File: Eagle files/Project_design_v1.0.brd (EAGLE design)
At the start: 100 x 80 mm, 4 parts

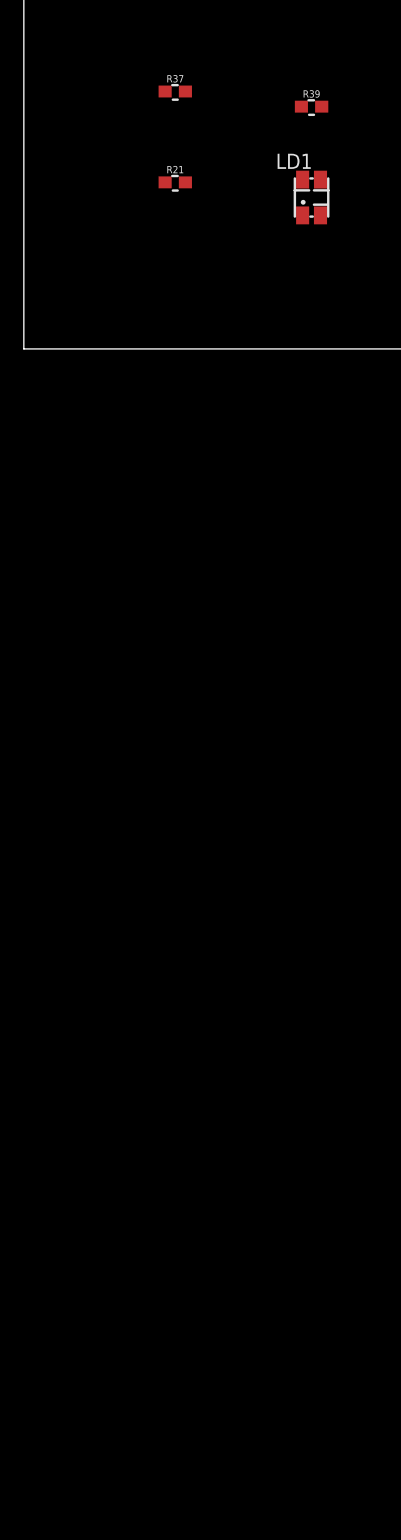
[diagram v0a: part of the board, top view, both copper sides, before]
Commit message: schematic des temperature, soil moisture, led, brightness sensor
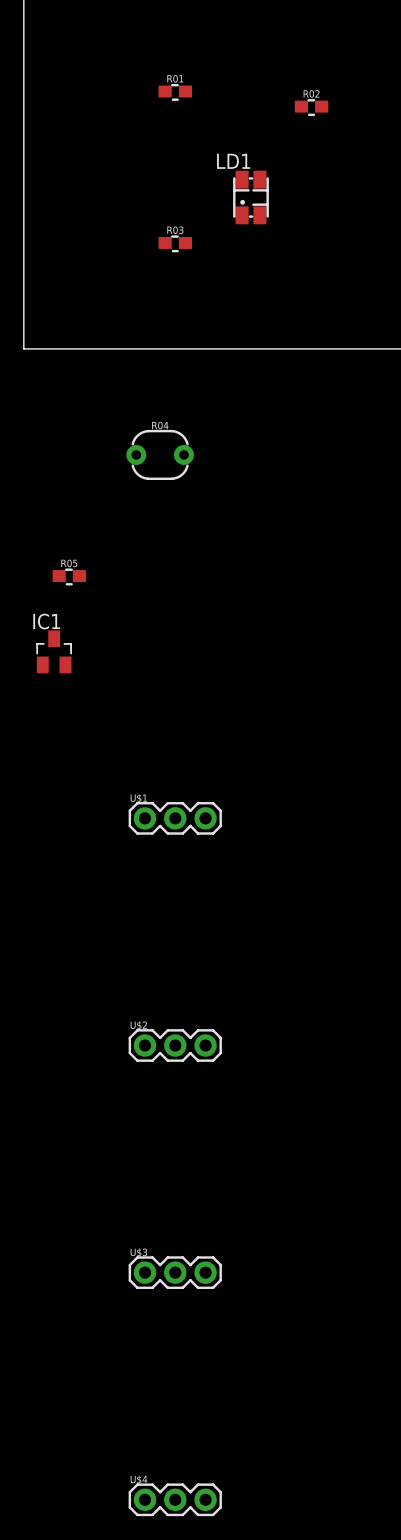
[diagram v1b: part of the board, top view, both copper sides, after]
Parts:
- removed R21: OR, custom_part:0603
- added IC1: LM50, linear:SOT23
- added R03: 2K, custom_part:0603
- added R04: PHOTOCELLPTH, SparkFun-Sensors:PHOTOCELL
- added R05: 10K, custom_part:0603
- added U$1, U$2, U$3, U$4: SOIL_MOISTURE, potentiometer:SOIL_MOISTURE
- R01: value 100R -> 3K
- R02: value 100R -> 2K
- moved LD1 5.08 mm to (19.1, 12.7)
- renumbered R37 to R01, R39 to R02
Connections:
- removed net MUX_DIS: R21.2
- new net GND: R05.1
- new net MOISTURE1: U$1.3
- new net MOISTURE2: U$2.3
- new net MOISTURE3: U$3.3
- new net MOISTURE4: U$4.3
- new net N$1: LD1.2, R03.1
- new net N$2: U$1.2
- new net N$3: U$2.2
- new net N$4: IC1.3
- new net N$5: U$3.2
- new net N$6: U$4.2
- new net PHOTOCELL_READ: R04.1, R05.2
- new net TEMP_READ: IC1.2
- net 3.3V: now also IC1.1, R04.2, U$1.1, U$2.1, U$3.1, U$4.1
- net LED_B: now also R03.2; no longer LD1.2
- net LED_R: no longer R21.1
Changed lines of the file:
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@@
 </autorouter>
 <elements>
-<element name="LD1" library="Semicond" package="PLCC-4" value="ASMB-MTB0-0A3A2PLCC-4" x="24.13" y="12.7">
-<attribute name="CODE" value="2401105" x="24.13" y="12.7" size="1.778" layer="27" display="off"/>
-<attribute name="DISTRIBUTOR" value="Farnell" x="24.13" y="12.7" size="1.778" layer="27" display="off"/>
-<attribute name="LINK" value="http://ch.farnell.com/fr-CH/broadcom-limited/asmb-mtb0-0a3a2/led-rgb-plcc4-surface-noire/dp/2401105" x="24.13" y="12.7" size="1.778" layer="27" display="off"/>
-<attribute name="PARTNO" value="ASMB-MTB0-0A3A2" x="24.13" y="12.7" size="1.778" layer="27" display="off"/>
-<attribute name="REFERENCE" value="ASMB-MTB0-0A3A2" x="24.13" y="12.7" size="1.778" layer="27" display="off"/>
-<attribute name="UNIT_PRICE" value="0.332" x="24.13" y="12.7" size="1.778" layer="27" display="off"/>
+<element name="LD1" library="Semicond" package="PLCC-4" value="ASMB-MTB0-0A3A2PLCC-4" x="19.05" y="12.7">
+<attribute name="CODE" value="2401105" x="19.05" y="12.7" size="1.778" layer="27" display="off"/>
+<attribute name="DISTRIBUTOR" value="Farnell" x="19.05" y="12.7" size="1.778" layer="27" display="off"/>
+<attribute name="LINK" value="http://ch.farnell.com/fr-CH/broadcom-limited/asmb-mtb0-0a3a2/led-rgb-plcc4-surface-noire/dp/2401105" x="19.05" y="12.7" size="1.778" layer="27" display="off"/>
+<attribute name="PARTNO" value="ASMB-MTB0-0A3A2" x="19.05" y="12.7" size="1.778" layer="27" display="off"/>
+<attribute name="REFERENCE" value="ASMB-MTB0-0A3A2" x="19.05" y="12.7" size="1.778" layer="27" display="off"/>
+<attribute name="UNIT_PRICE" value="0.332" x="19.05" y="12.7" size="1.778" layer="27" display="off"/>
 </element>
-<element name="R21" library="custom_part" package="0603" value="OR" x="12.7" y="13.97">
-<attribute name="PARTNO" value="ERJ-PA3F1002V" x="12.7" y="13.97" size="1.778" layer="27" display="off"/>
-</element>
-<element name="R37" library="custom_part" package="0603" value="100R" x="12.7" y="21.59">
+<element name="R01" library="custom_part" package="0603" value="3K" x="12.7" y="21.59">
 <attribute name="PARTNO" value="ERJ-PA3F1002V" x="12.7" y="21.59" size="1.778" layer="27" display="off"/>
 </element>
-<element name="R39" library="custom_part" package="0603" value="100R" x="24.13" y="20.32">
+<element name="R02" library="custom_part" package="0603" value="2K" x="24.13" y="20.32">
 <attribute name="PARTNO" value="ERJ-PA3F1002V" x="24.13" y="20.32" size="1.778" layer="27" display="off"/>
 </element>
+<element name="R03" library="custom_part" package="0603" value="2K" x="12.7" y="8.89">
+<attribute name="PARTNO" value="ERJ-PA3F1002V" x="12.7" y="8.89" size="1.778" layer="27" display="off"/>
+</element>
+<element name="R04" library="SparkFun-Sensors" library_urn="urn:adsk.eagle:library:534" package="PHOTOCELL" package3d_urn="urn:adsk.eagle:package:39940/1" value="PHOTOCELLPTH" x="11.43" y="-8.89">
+<attribute name="PROD_ID" value="COMP-09129" x="11.43" y="-8.89" size="1.778" layer="27" display="off"/>
+<attribute name="SF_ID" value="SEN-09088" x="11.43" y="-8.89" size="1.778" layer="27" display="off"/>
+</element>
+<element name="R05" library="custom_part" package="0603" value="10K" x="3.81" y="-19.05">
+<attribute name="PARTNO" value="ERJ-PA3F1002V" x="3.81" y="-19.05" size="1.778" layer="27" display="off"/>
+</element>
+<element name="IC1" library="linear" library_urn="urn:adsk.eagle:library:262" package="SOT23" package3d_urn="urn:adsk.eagle:package:16489/2" value="LM50" x="2.54" y="-25.4"/>
+<element name="U$1" library="potentiometer" package="SOIL_MOISTURE" value="SOIL_MOISTURE" x="12.7" y="-39.37"/>
+<element name="U$2" library="potentiometer" package="SOIL_MOISTURE" value="SOIL_MOISTURE" x="12.7" y="-58.42"/>
+<element name="U$3" library="potentiometer" package="SOIL_MOISTURE" value="SOIL_MOISTURE" x="12.7" y="-77.47"/>
+<element name="U$4" library="potentiometer" package="SOIL_MOISTURE" value="SOIL_MOISTURE" x="12.7" y="-96.52"/>
 </elements>
 <signals>
 <signal name="3.3V">
 <contactref element="LD1" pad="1"/>
-</signal>
-<signal name="MUX_DIS">
-<contactref element="R21" pad="2"/>
+<contactref element="R04" pad="2"/>
+<contactref element="IC1" pad="1"/>
+<contactref element="U$1" pad="1"/>
+<contactref element="U$2" pad="1"/>
+<contactref element="U$3" pad="1"/>
+<contactref element="U$4" pad="1"/>
+<wire x1="10.16" y1="-77.47" x2="10.16" y2="-96.52" width="0" layer="19" extent="1-1"/>
+<wire x1="10.16" y1="-58.42" x2="10.16" y2="-77.47" width="0" layer="19" extent="1-1"/>
+<wire x1="10.16" y1="-39.37" x2="10.16" y2="-58.42" width="0" layer="19" extent="1-1"/>
+<wire x1="1.59" y1="-26.5" x2="10.16" y2="-39.37" width="0" layer="19" extent="1-1"/>
+<wire x1="13.43" y1="-8.89" x2="1.59" y2="-26.5" width="0" layer="19" extent="1-1"/>
+<wire x1="18.3" y1="11.2" x2="13.43" y2="-8.89" width="0" layer="19" extent="1-1"/>
 </signal>
 <signal name="N$34">
 <contactref element="LD1" pad="3"/>
-<contactref element="R37" pad="1"/>
-<wire x1="11.85" y1="21.59" x2="24.88" y2="14.2" width="0" layer="19" extent="1-1"/>
+<contactref element="R01" pad="1"/>
+<wire x1="11.85" y1="21.59" x2="19.8" y2="14.2" width="0" layer="19" extent="1-1"/>
 </signal>
 <signal name="N$35">
 <contactref element="LD1" pad="4"/>
-<contactref element="R39" pad="1"/>
-<wire x1="23.28" y1="20.32" x2="24.88" y2="11.2" width="0" layer="19" extent="1-1"/>
+<contactref element="R02" pad="1"/>
+<wire x1="23.28" y1="20.32" x2="19.8" y2="11.2" width="0" layer="19" extent="1-1"/>
+</signal>
+<signal name="LED_G">
+<contactref element="R01" pad="2"/>
+</signal>
+<signal name="LED_R">
+<contactref element="R02" pad="2"/>
+</signal>
+<signal name="N$1">
+<contactref element="LD1" pad="2"/>
+<contactref element="R03" pad="1"/>
+<wire x1="11.85" y1="8.89" x2="18.3" y2="14.2" width="0" layer="19" extent="1-1"/>
 </signal>
 <signal name="LED_B">
-<contactref element="LD1" pad="2"/>
+<contactref element="R03" pad="2"/>
 </signal>
-<signal name="LED_G">
-<contactref element="R37" pad="2"/>
+<signal name="PHOTOCELL_READ">
+<contactref element="R05" pad="2"/>
+<contactref element="R04" pad="1"/>
+<wire x1="9.43" y1="-8.89" x2="4.66" y2="-19.05" width="0" layer="19" extent="1-1"/>
 </signal>
-<signal name="LED_R">
-<contactref element="R39" pad="2"/>
-<contactref element="R21" pad="1"/>
-<wire x1="11.85" y1="13.97" x2="24.98" y2="20.32" width="0" layer="19" extent="1-1"/>
+<signal name="GND">
+<contactref element="R05" pad="1"/>
+</signal>
+<signal name="TEMP_READ">
+<contactref element="IC1" pad="2"/>
+</signal>
+<signal name="N$4">
+<contactref element="IC1" pad="3"/>
+</signal>
+<signal name="N$2">
+<contactref element="U$1" pad="2"/>
+</signal>
+<signal name="MOISTURE1">
+<contactref element="U$1" pad="3"/>
+</signal>
+<signal name="N$3">
+<contactref element="U$2" pad="2"/>
+</signal>
+<signal name="N$5">
+<contactref element="U$3" pad="2"/>
+</signal>
+<signal name="N$6">
+<contactref element="U$4" pad="2"/>
+</signal>
+<signal name="MOISTURE3">
+<contactref element="U$3" pad="3"/>
+</signal>
+<signal name="MOISTURE4">
+<contactref element="U$4" pad="3"/>
+</signal>
+<signal name="MOISTURE2">
+<contactref element="U$2" pad="3"/>
 </signal>
 </signals>
 </board>
 </drawing>
+<compatibility>
+<note version="8.2" severity="warning">
+Since Version 8.2, EAGLE supports online libraries. The ids
+of those online libraries will not be understood (or retained)
+with this version.
+</note>
+<note version="8.3" severity="warning">
+Since Version 8.3, EAGLE supports URNs for individual library
+assets (packages, symbols, and devices). The URNs of those assets
+will not be understood (or retained) with this version.
+</note>
+<note version="8.3" severity="warning">
+Since Version 8.3, EAGLE supports the association of 3D packages
+with devices in libraries, schematics, and board files. Those 3D
+packages will not be understood (or retained) with this version.
+</note>
+</compatibility>
 </eagle>

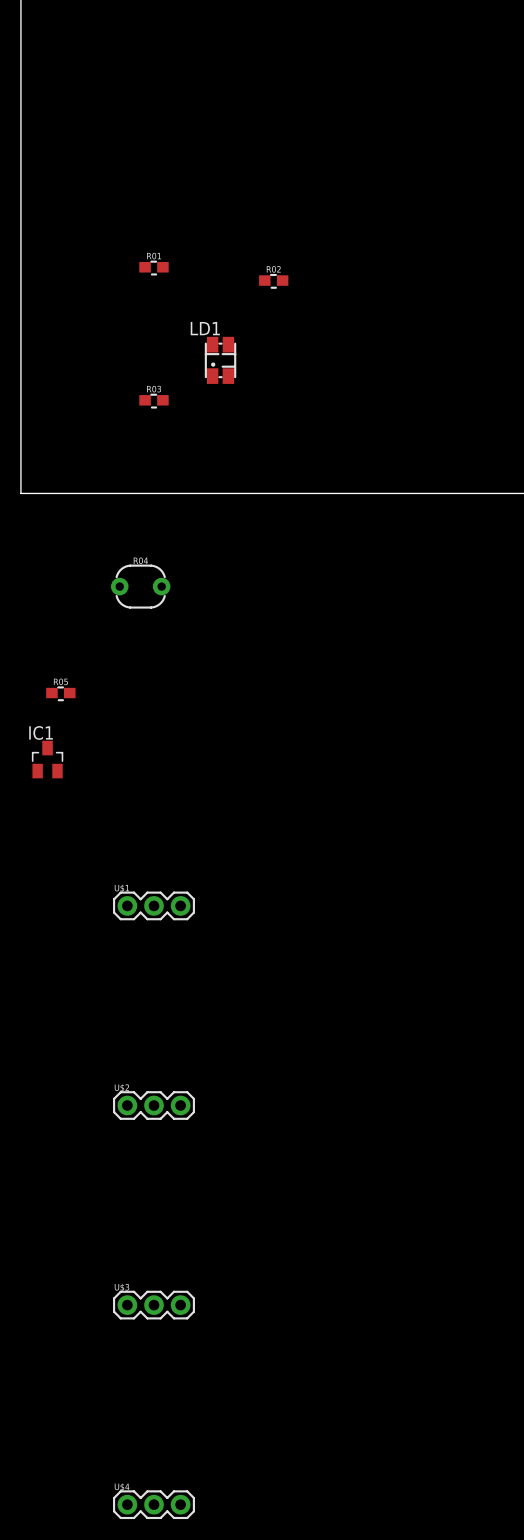
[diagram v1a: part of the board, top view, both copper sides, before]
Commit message: temperature sensor schmetatic & packages edited
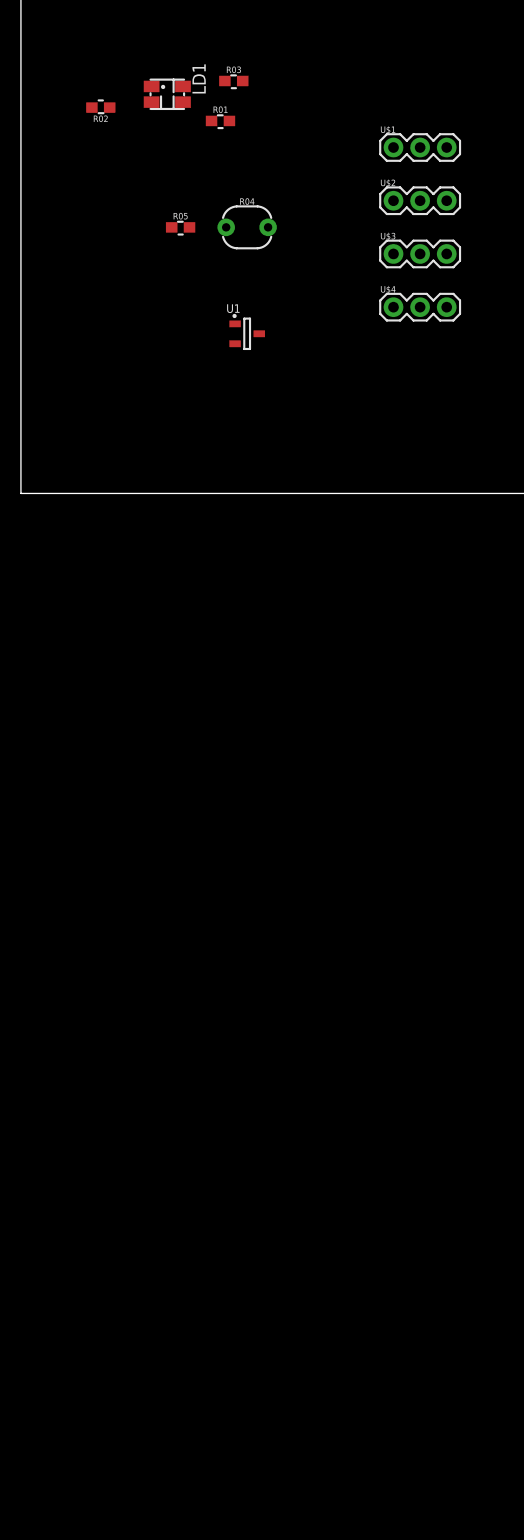
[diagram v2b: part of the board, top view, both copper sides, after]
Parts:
- removed IC1: LM50, linear:SOT23
- added U1: MCP9700T-E/TT, MCP9700T-E_TT:SOT95P237X112-3N
- moved U$4 117.1 mm to (38.1, 17.8)
- moved U$3 103.5 mm to (38.1, 22.9)
- moved U$2 90.0 mm to (38.1, 27.9)
- moved U$1 76.7 mm to (38.1, 33.0)
- moved R05 45.9 mm to (15.2, 25.4)
- moved R04 35.8 mm to (21.6, 25.4)
- moved R03 31.4 mm to (20.3, 39.4)
- moved LD1 25.9 mm to (14.0, 38.1), turned to 270 degrees
- moved R02 23.3 mm to (7.62, 36.8), turned to 180 degrees
- moved R01 15.3 mm to (19.1, 35.6)
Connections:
- removed net N$2: U$1.2
- removed net N$3: U$2.2
- removed net N$4: IC1.3
- removed net N$5: U$3.2
- removed net N$6: U$4.2
- net 3.3V: now also U1.1; no longer IC1.1
- net GND: now also U$1.2, U$2.2, U$3.2, U$4.2, U1.3
- net TEMP_READ: now also U1.2; no longer IC1.2

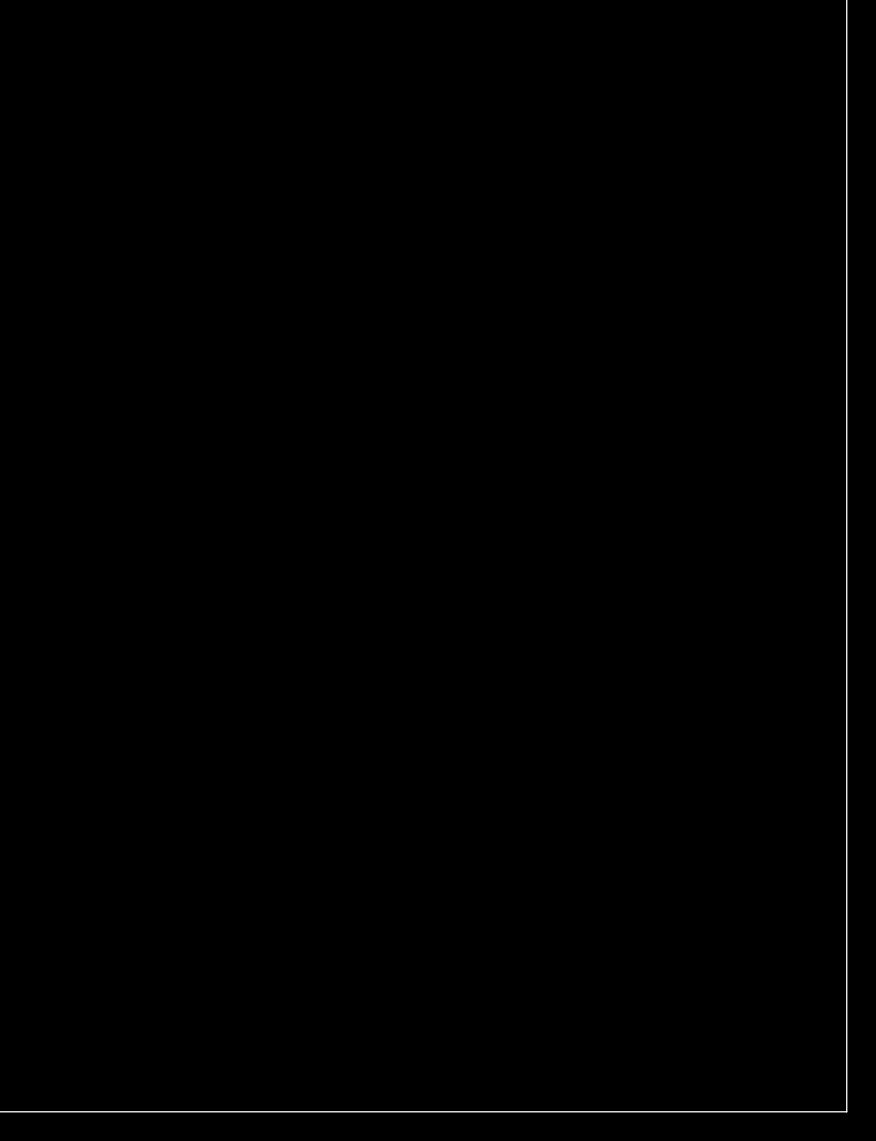
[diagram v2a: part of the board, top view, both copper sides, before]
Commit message: MCU, charging IC & power supply implemented on the eagle schematics
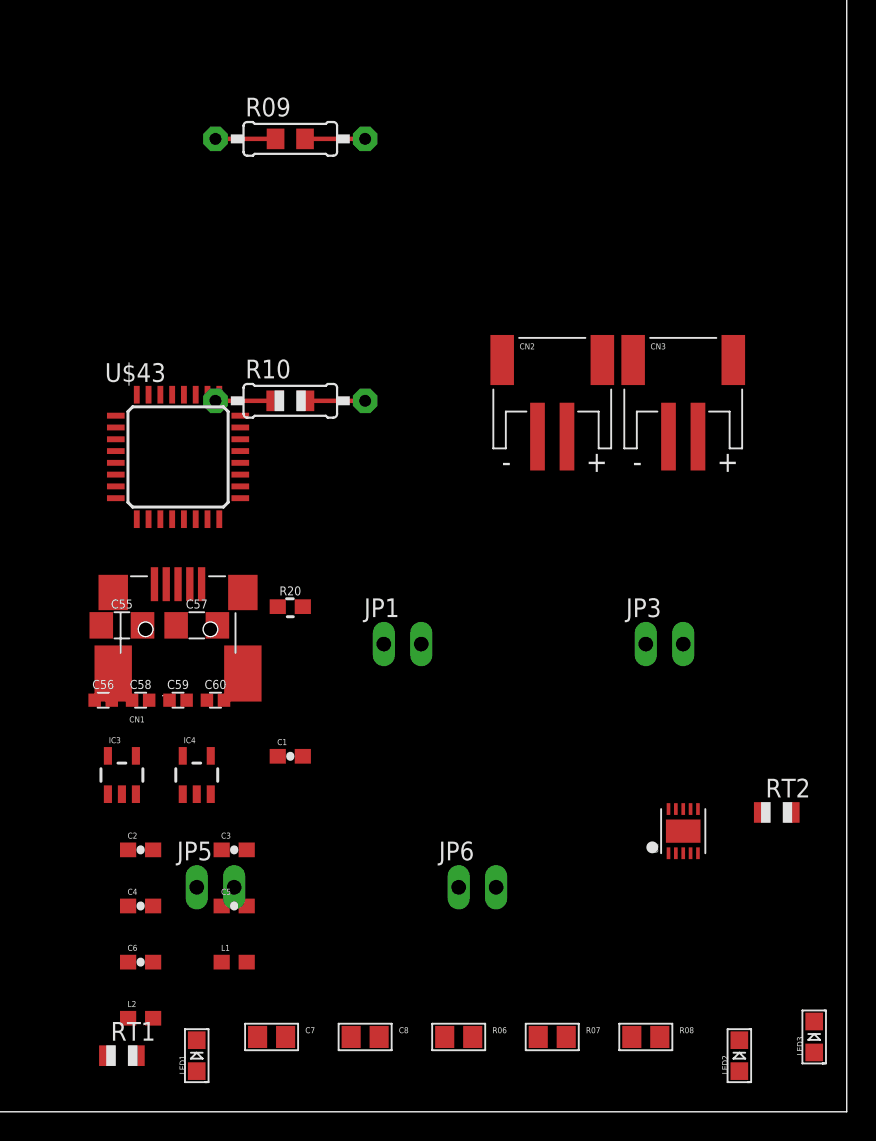
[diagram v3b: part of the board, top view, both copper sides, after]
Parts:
- added C1, C4: 2.2uF, SparkFun-Passives:0603-CAP
- added C2, C3, C5, C6: 10uF, SparkFun-Passives:0603-CAP
- added C55, C57: 10uF, custom_part:1206
- added C56, C58, C59, C60: 100n, custom_part:0402
- added C7, C8: 10uF, microbuilder:0805
- added CN1: USB, microbuilder:USB-MINIB_LARGER
- added CN2: BATT_IN_JST, microbuilder:JSTPH2
- added CN3: LOAD_JST, microbuilder:JSTPH2
- added IC3: TPS73250DBVT, TPS32xx:SOT23-5
- added IC4: TPS73233DBVT, TPS32xx:SOT23-5
- added JP1: PWR_IN_0.1, microbuilder:1X02_OVAL
- added JP3: LOAD_0.1, microbuilder:1X02_OVAL
- added JP5: BATT_IN_0.1, microbuilder:1X02_OVAL
- added JP6: STAT, microbuilder:1X02_OVAL
- added L1, L2: 3.3 uH, SparkFun-Passives:0603
- added LED1: STAT1-ORANGE, microbuilder:CHIPLED_0805
- added LED2: STAT2-GREEN, microbuilder:CHIPLED_0805
- added LED3: Power-RED, microbuilder:CHIPLED_0805
- added R06, R07, R08: 150, microbuilder:0805
- added R09: PROG, microbuilder:0805-THM
- added R10: 10K/THERM, adafruit:0805-THM
- added R20: 10K, custom_part:0603
- added RT1: 1K, adafruit:R0805
- added RT2: 150K, adafruit:R0805
- added U$43: STM32F042K6T6, stm32-microcontrollers:LQFP32-7X7
- added U2: MCP73833T-AMI/MF, microbuilder:DFN10_3X3MM
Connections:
- new net 5.0V: C7.1, CN1.VBUS, JP1.2, LED1.A, LED2.A, LED3.A, U2.P$1, U2.P$2
- new net 5V: IC3.1, IC3.3, IC4.1, IC4.3
- new net AGND: C1.2, C2.2, C3.2, C4.2, C5.2, C6.2, IC3.2, IC4.2
- new net AVDD: C3.1, C60.1, L1.2, U$43.5
- new net BATT: C8.1, CN2.2, CN3.2, JP3.2, JP5.2, U2.P$10, U2.P$9
- new net BOOT0: R20.2, U$43.31
- new net CHARGE_CMD: U$43.11
- new net DAC_CLK: U$43.12
- new net DAC_D2: U$43.13
- new net DAC_D3: U$43.18
- new net DAC_D4: U$43.19
- new net DAC_D5: U$43.20
- new net DAC_D6: U$43.21
- new net DAC_D7: U$43.22
- new net DAC_D8: U$43.25
- new net DVDD: C6.1, L2.2
- new net HV_DONE: U$43.10
- new net LI_PRESET: U$43.2
- new net LOAD_CURRENT_1: U$43.6
- new net LOAD_CURRENT_2: U$43.7
- new net LOAD_CURRENT_3: U$43.8
- new net LOAD_CURRENT_4: U$43.9
- new net MUX_DIS: U$43.28
- new net MUX_IN: U$43.14
- new net MUX_S0: U$43.15
- new net MUX_S1: U$43.26
- new net MUX_S2: U$43.27
- new net N$12: LED3.C, R08.1
- new net N$13: C1.1, C2.1, IC3.5, L1.1
- new net N$16: R09.2, U2.P$6
- new net N$2: C4.1, C5.1, IC4.5, L2.1
- new net N$3: LED1.C, R06.2
- new net N$4: LED2.C, R07.2
- new net N$5: JP6.1, R06.1, U2.P$3
- new net N$6: JP6.2, R07.1, U2.P$4
- new net N$7: R08.2, U2.P$7
- new net N$8: RT1.1, U2.P$8
- new net N$9: R10.2, RT1.2, RT2.2
- new net NRST: C59.1, U$43.4
- new net SWCLK: U$43.24
- new net SWDIO: U$43.23
- new net USART1_RX/I2C1_SDA: U$43.30
- new net USART1_TX/I2C1_SCL: U$43.29
- net 3.3V: now also C55.1, C56.1, C57.1, C58.1, U$43.1, U$43.17
- net GND: now also C55.2, C56.2, C57.2, C58.2, C59.2, C60.2, C7.2, C8.2, CN1.GND, CN2.1, CN3.1, JP1.1, JP3.1, JP5.1, R09.1, R10.1, R20.1, RT2.1, U$43.16, U$43.32, U2.P$5
- net LED_G: now also U$43.3
